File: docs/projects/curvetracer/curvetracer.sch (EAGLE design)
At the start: 9 parts, among them IC2 MC33201

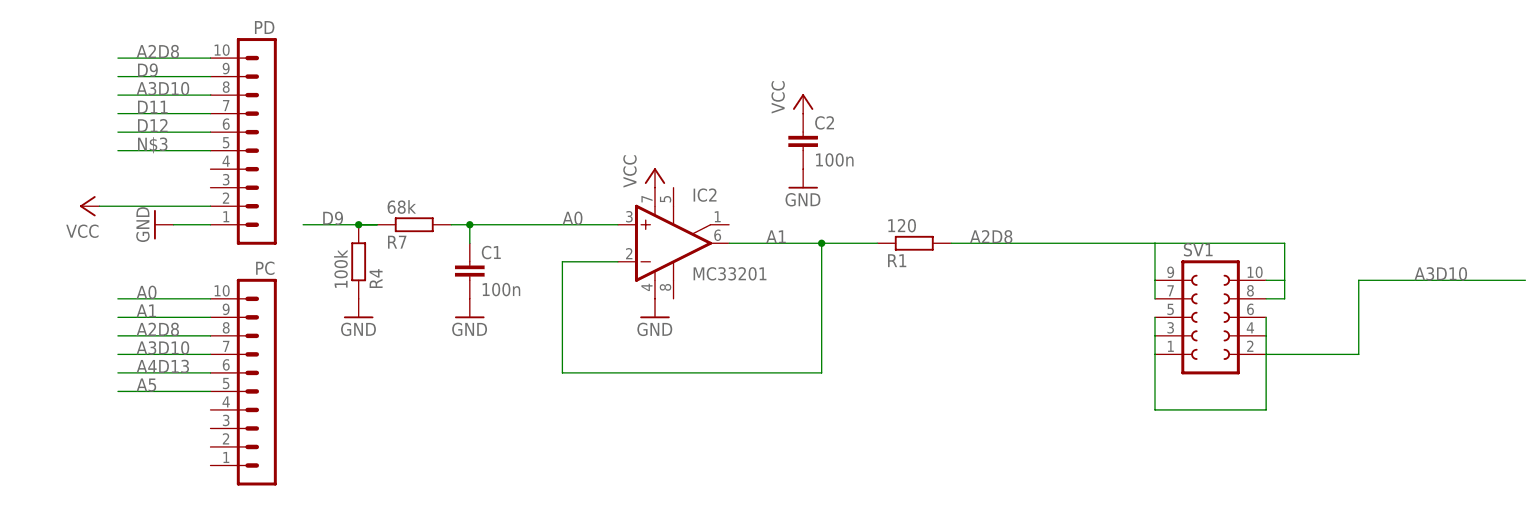
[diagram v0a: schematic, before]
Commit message: support for voltagetransfer
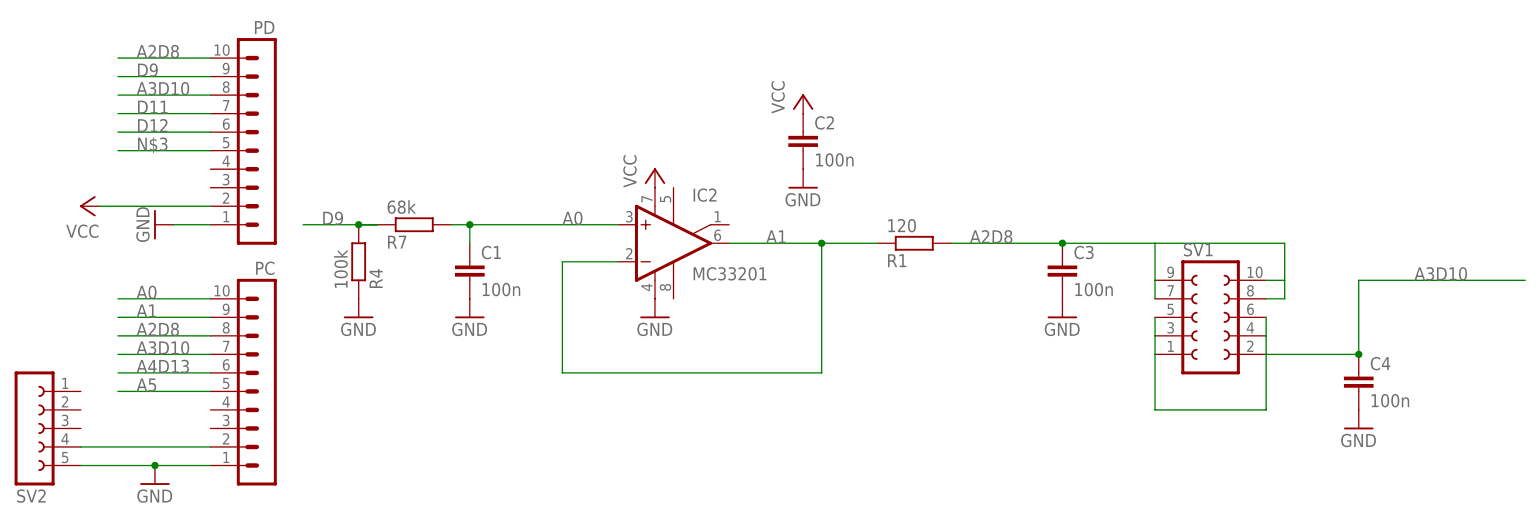
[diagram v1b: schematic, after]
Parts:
- added C3: 100n, rcl:C-EU075-032X103
- added C4: 100n, rcl:C-EU102-043X133
- added SV2: (no value), con-lsta:FE05W
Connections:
- new net N$1: PC.2, SV2.4
- net A2D8: now also C3.1
- net A3D10: now also C4.1
- net GND: now also C3.2, C4.2, PC.1, SV2.5
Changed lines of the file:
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@@
 <?xml version="1.0" encoding="utf-8"?>
 <!DOCTYPE eagle SYSTEM "eagle.dtd">
-<eagle version="6.2">
+<eagle version="6.4">
 <drawing>
 <settings>
@@
 <grid distance="0.1" unitdist="inch" unit="inch" style="lines" multiple="1" display="no" altdistance="0.01" altunitdist="inch" altunit="inch"/>
 <layers>
-<layer number="1" name="Top" color="4" fill="1" visible="no" active="no"/>
-<layer number="16" name="Bottom" color="1" fill="1" visible="no" active="no"/>
-<layer number="17" name="Pads" color="2" fill="1" visible="no" active="no"/>
-<layer number="18" name="Vias" color="2" fill="1" visible="no" active="no"/>
-<layer number="19" name="Unrouted" color="6" fill="1" visible="no" active="no"/>
-<layer number="20" name="Dimension" color="15" fill="1" visible="no" active="no"/>
-<layer number="21" name="tPlace" color="7" fill="1" visible="no" active="no"/>
-<layer number="22" name="bPlace" color="7" fill="1" visible="no" active="no"/>
-<layer number="23" name="tOrigins" color="15" fill="1" visible="no" active="no"/>
-<layer number="24" name="bOrigins" color="15" fill="1" visible="no" active="no"/>
-<layer number="25" name="tNames" color="7" fill="1" visible="no" active="no"/>
-<layer number="26" name="bNames" color="7" fill="1" visible="no" active="no"/>
-<layer number="27" name="tValues" color="7" fill="1" visible="no" active="no"/>
-<layer number="28" name="bValues" color="7" fill="1" visible="no" active="no"/>
+<layer number="1" name="Top" color="4" fill="1" visible="yes" active="no"/>
+<layer number="16" name="Bottom" color="1" fill="1" visible="yes" active="no"/>
+<layer number="17" name="Pads" color="2" fill="1" visible="yes" active="no"/>
+<layer number="18" name="Vias" color="2" fill="1" visible="yes" active="no"/>
+<layer number="19" name="Unrouted" color="6" fill="1" visible="yes" active="no"/>
+<layer number="20" name="Dimension" color="15" fill="1" visible="yes" active="no"/>
+<layer number="21" name="tPlace" color="7" fill="1" visible="yes" active="no"/>
+<layer number="22" name="bPlace" color="7" fill="1" visible="yes" active="no"/>
+<layer number="23" name="tOrigins" color="15" fill="1" visible="yes" active="no"/>
+<layer number="24" name="bOrigins" color="15" fill="1" visible="yes" active="no"/>
+<layer number="25" name="tNames" color="7" fill="1" visible="yes" active="no"/>
+<layer number="26" name="bNames" color="7" fill="1" visible="yes" active="no"/>
+<layer number="27" name="tValues" color="7" fill="1" visible="yes" active="no"/>
+<layer number="28" name="bValues" color="7" fill="1" visible="yes" active="no"/>
 <layer number="29" name="tStop" color="7" fill="3" visible="no" active="no"/>
 <layer number="30" name="bStop" color="7" fill="6" visible="no" active="no"/>
@@
 <layer number="35" name="tGlue" color="7" fill="4" visible="no" active="no"/>
 <layer number="36" name="bGlue" color="7" fill="5" visible="no" active="no"/>
-<layer number="37" name="tTest" color="7" fill="1" visible="no" active="no"/>
-<layer number="38" name="bTest" color="7" fill="1" visible="no" active="no"/>
+<layer number="37" name="tTest" color="7" fill="1" visible="yes" active="no"/>
+<layer number="38" name="bTest" color="7" fill="1" visible="yes" active="no"/>
 <layer number="39" name="tKeepout" color="4" fill="11" visible="no" active="no"/>
 <layer number="40" name="bKeepout" color="1" fill="11" visible="no" active="no"/>
@@
 <layer number="44" name="Drills" color="7" fill="1" visible="no" active="no"/>
 <layer number="45" name="Holes" color="7" fill="1" visible="no" active="no"/>
-<layer number="46" name="Milling" color="3" fill="1" visible="no" active="no"/>
-<layer number="47" name="Measures" color="7" fill="1" visible="no" active="no"/>
-<layer number="48" name="Document" color="7" fill="1" visible="no" active="no"/>
-<layer number="49" name="Reference" color="7" fill="1" visible="no" active="no"/>
-<layer number="50" name="dxf" color="7" fill="1" visible="no" active="no"/>
-<layer number="51" name="tDocu" color="7" fill="1" visible="no" active="no"/>
-<layer number="52" name="bDocu" color="7" fill="1" visible="no" active="no"/>
+<layer number="46" name="Milling" color="3" fill="1" visible="yes" active="no"/>
+<layer number="47" name="Measures" color="7" fill="1" visible="yes" active="no"/>
+<layer number="48" name="Document" color="7" fill="1" visible="yes" active="no"/>
+<layer number="49" name="Reference" color="7" fill="1" visible="yes" active="no"/>
+<layer number="50" name="dxf" color="7" fill="1" visible="yes" active="no"/>
+<layer number="51" name="tDocu" color="7" fill="1" visible="yes" active="no"/>
+<layer number="52" name="bDocu" color="7" fill="1" visible="yes" active="no"/>
 <layer number="91" name="Nets" color="2" fill="1" visible="yes" active="yes"/>
 <layer number="92" name="Busses" color="1" fill="1" visible="yes" active="yes"/>
@@
 <part name="P+4" library="supply1" deviceset="VCC" device=""/>
 <part name="GND4" library="supply1" deviceset="GND" device=""/>
+<part name="SV2" library="con-lsta" deviceset="FE05W" device=""/>
+<part name="C3" library="rcl" deviceset="C-EU" device="075-032X103" value="100n"/>
+<part name="C4" library="rcl" deviceset="C-EU" device="102-043X133" value="100n"/>
+<part name="GND2" library="supply1" deviceset="GND" device=""/>
+<part name="GND7" library="supply1" deviceset="GND" device=""/>
+<part name="GND8" library="supply1" deviceset="GND" device=""/>
 </parts>
 <sheets>
@@
 <instance part="P+4" gate="VCC" x="210.82" y="119.38"/>
 <instance part="GND4" gate="1" x="210.82" y="106.68"/>
+<instance part="SV2" gate="G$1" x="104.14" y="73.66" rot="MR180"/>
+<instance part="C3" gate="G$1" x="246.38" y="96.52"/>
+<instance part="C4" gate="G$1" x="287.02" y="81.28"/>
+<instance part="GND2" gate="1" x="246.38" y="88.9"/>
+<instance part="GND7" gate="1" x="287.02" y="73.66"/>
+<instance part="GND8" gate="1" x="121.92" y="66.04"/>
 </instances>
 <busses>
@@
 <pinref part="GND4" gate="1" pin="GND"/>
 </segment>
+<segment>
+<pinref part="C3" gate="G$1" pin="2"/>
+<pinref part="GND2" gate="1" pin="GND"/>
+</segment>
+<segment>
+<pinref part="C4" gate="G$1" pin="2"/>
+<pinref part="GND7" gate="1" pin="GND"/>
+</segment>
+<segment>
+<pinref part="PC" gate="1" pin="1"/>
+<pinref part="SV2" gate="G$1" pin="5"/>
+<wire x1="129.54" y1="68.58" x2="121.92" y2="68.58" width="0.1524" layer="91"/>
+<pinref part="GND8" gate="1" pin="GND"/>
+<wire x1="121.92" y1="68.58" x2="111.76" y2="68.58" width="0.1524" layer="91"/>
+<junction x="121.92" y="68.58"/>
+</segment>
 </net>
 <net name="A2D8" class="0">
@@
 <wire x1="259.08" y1="91.44" x2="259.08" y2="93.98" width="0.1524" layer="91"/>
 <wire x1="259.08" y1="93.98" x2="259.08" y2="99.06" width="0.1524" layer="91"/>
-<wire x1="259.08" y1="99.06" x2="231.14" y2="99.06" width="0.1524" layer="91"/>
+<wire x1="259.08" y1="99.06" x2="246.38" y2="99.06" width="0.1524" layer="91"/>
+<wire x1="246.38" y1="99.06" x2="231.14" y2="99.06" width="0.1524" layer="91"/>
 <wire x1="259.08" y1="99.06" x2="276.86" y2="99.06" width="0.1524" layer="91"/>
 <wire x1="276.86" y1="99.06" x2="276.86" y2="93.98" width="0.1524" layer="91"/>
@@
 <pinref part="SV1" gate="G$1" pin="8"/>
 <pinref part="SV1" gate="G$1" pin="10"/>
+<pinref part="C3" gate="G$1" pin="1"/>
+<junction x="246.38" y="99.06"/>
 </segment>
 <segment>
@@
 <pinref part="SV1" gate="G$1" pin="3"/>
 <pinref part="SV1" gate="G$1" pin="5"/>
+<pinref part="C4" gate="G$1" pin="1"/>
+<junction x="287.02" y="83.82"/>
 </segment>
 <segment>
@@
 </segment>
 </net>
+<net name="N$1" class="0">
+<segment>
+<pinref part="SV2" gate="G$1" pin="4"/>
+<pinref part="PC" gate="1" pin="2"/>
+<wire x1="111.76" y1="71.12" x2="129.54" y2="71.12" width="0.1524" layer="91"/>
+</segment>
+</net>
